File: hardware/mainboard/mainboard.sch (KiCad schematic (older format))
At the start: 29 parts, among them J1 2309407-1, J3 Conn_01x02_Male, J4 3-84953-0, J5 503182-1852, U2 MIC5504-1.2YM5-TR, U5 ICM-20602

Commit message: start on v0.2
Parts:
- J4: footprint mainboard:TE_3-84953-0 -> mainboard:68713014522
- U3: renamed from U?; footprint DFN8_2x3MC_MCH -> mainboard:MCP1725-ADJE_MC
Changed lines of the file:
@@
 NoConn ~ 2750 1100
 NoConn ~ 2750 1200
-Text Notes 7350 4600 0    50   ~ 0
+Text Notes 6200 7900 0    50   ~ 0
 OV13850 FPC Conn\n
 $Comp
@@
 F 0 "J4" H 6980 6046 50  0000 L CNN
 F 1 "3-84953-0" H 6980 5955 50  0000 L CNN
-F 2 "mainboard:TE_3-84953-0" H 6750 6050 50  0001 L BNN
+F 2 "mainboard:68713014522" H 6750 6050 50  0001 L BNN
 F 3 "3-84953-0" H 6750 6050 50  0001 L BNN
 F 4 "Compliant" H 6750 6050 50  0001 L BNN "Field4"
@@
 NoConn ~ 10500 7150
 $Comp
-L power:GND #PWR?
+L power:GND #PWR0235
 U 1 1 5FA58E8D
 P 8500 7450
-F 0 "#PWR?" H 8500 7200 50  0001 C CNN
+F 0 "#PWR0235" H 8500 7200 50  0001 C CNN
 F 1 "GND" H 8505 7277 50  0000 C CNN
 F 2 "" H 8500 7450 50  0001 C CNN
@@
 	8500 7150 8500 7250
 $Comp
-L mainboard:MCP1725-ADJE_MC U?
+L mainboard:MCP1725-ADJE_MC U3
 U 1 1 5F9F70E9
 P 8500 7150
-F 0 "U?" H 9500 7537 60  0000 C CNN
+F 0 "U3" H 9500 7537 60  0000 C CNN
 F 1 "MCP1725-ADJE_MC" H 9500 7431 60  0000 C CNN
-F 2 "DFN8_2x3MC_MCH" H 9500 7390 60  0001 C CNN
+F 2 "mainboard:MCP1725-ADJE_MC" H 9500 7390 60  0001 C CNN
 F 3 "" H 8500 7150 60  0000 C CNN
 	1    8500 7150
@@
 $EndComp
 $Comp
-L power:+3.3V #PWR?
+L power:+3.3V #PWR0236
 U 1 1 5FB39ABE
 P 8150 7150
-F 0 "#PWR?" H 8150 7000 50  0001 C CNN
+F 0 "#PWR0236" H 8150 7000 50  0001 C CNN
 F 1 "+3.3V" V 8165 7278 50  0000 L CNN
 F 2 "" H 8150 7150 50  0001 C CNN
@@
 	11100 7100 11400 7100
 $Comp
-L power:GND #PWR?
+L power:GND #PWR0240
 U 1 1 5FBE8000
 P 11100 6900
-F 0 "#PWR?" H 11100 6650 50  0001 C CNN
+F 0 "#PWR0240" H 11100 6650 50  0001 C CNN
 F 1 "GND" H 11105 6727 50  0000 C CNN
 F 2 "" H 11100 6900 50  0001 C CNN

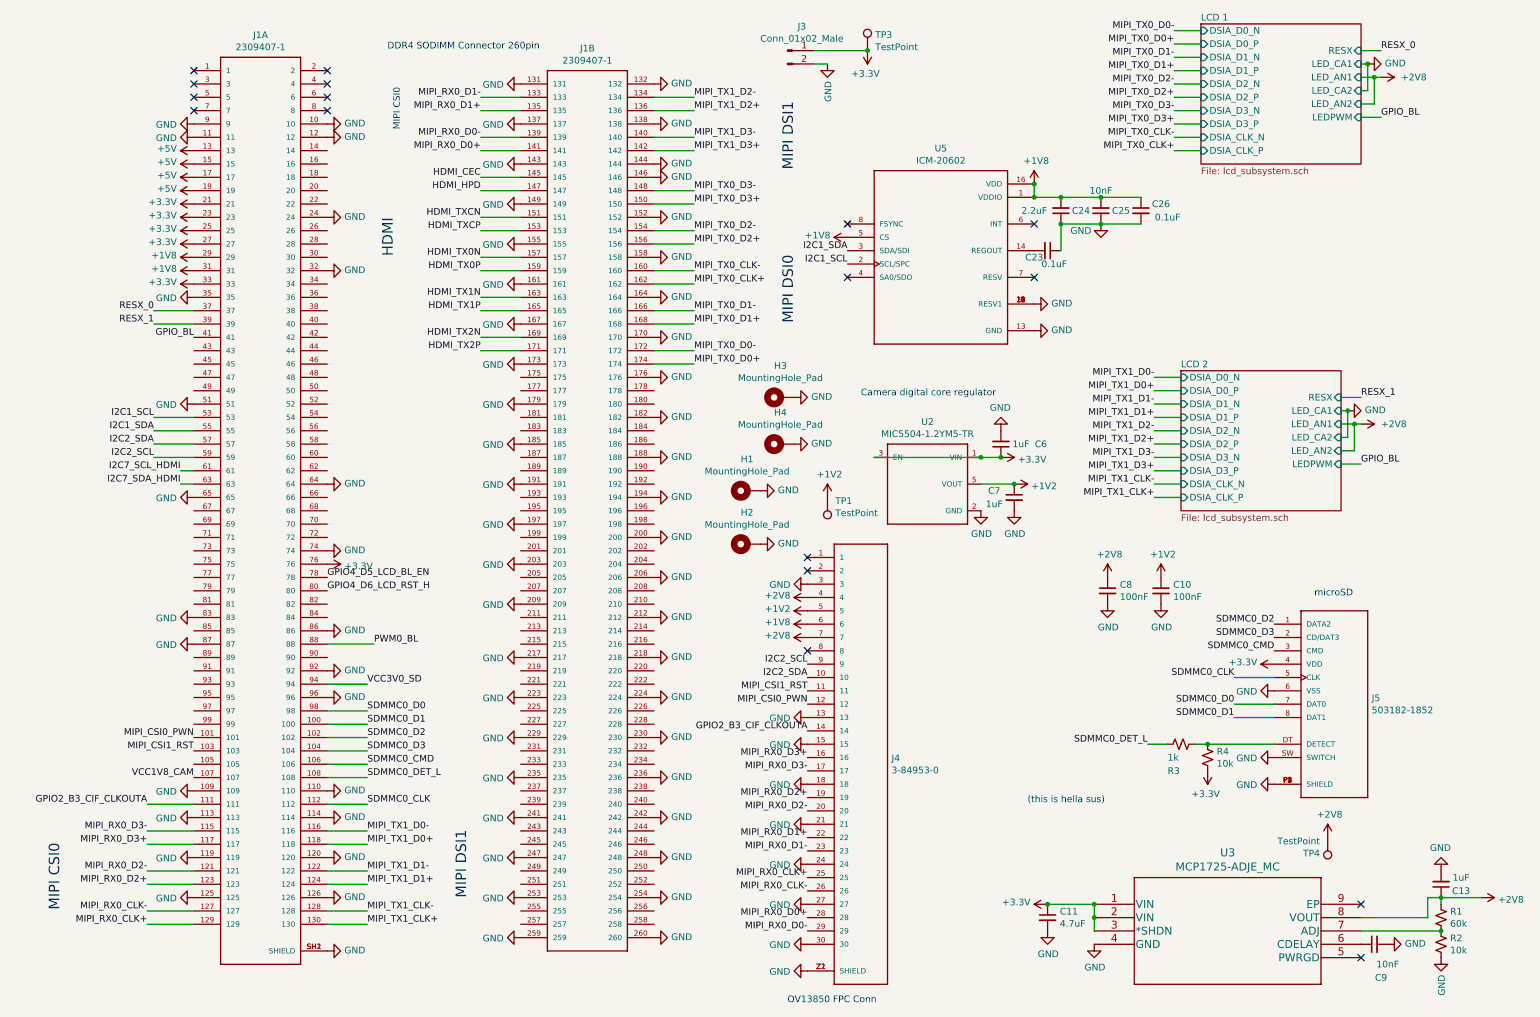
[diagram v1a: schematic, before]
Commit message: redesign started, symbol scripts, new dsi chip
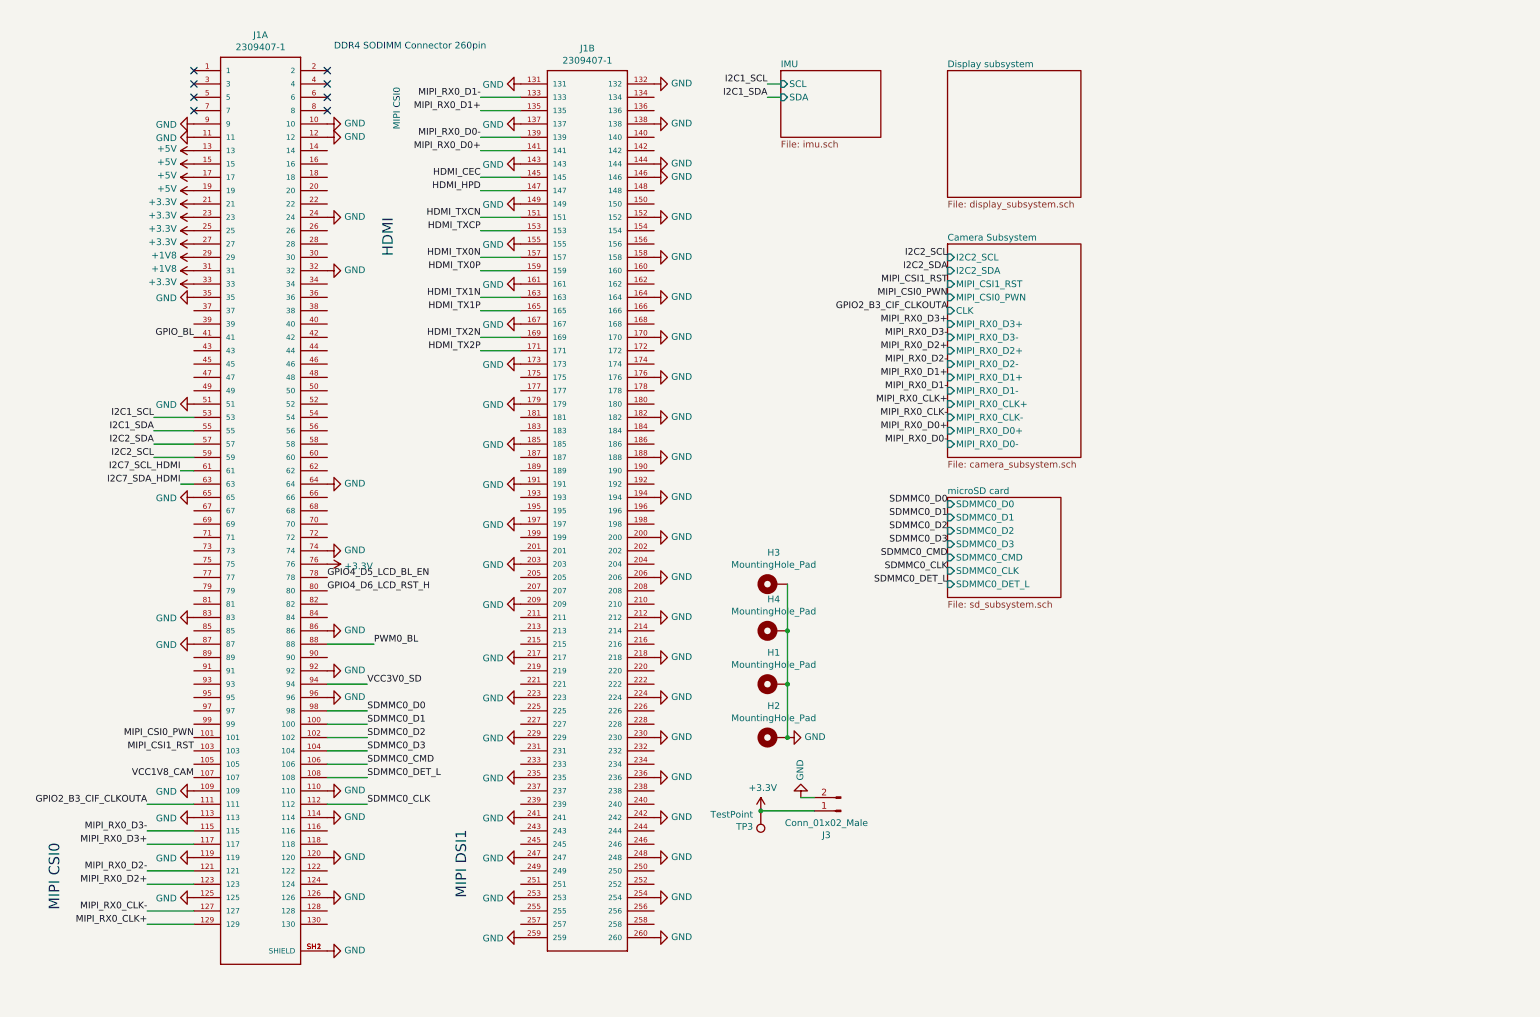
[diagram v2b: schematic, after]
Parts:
- removed C10, C8: 100nF, Capacitor_SMD:C_0402_1005Metric_Pad0.74x0.62mm_HandSolder, symbol Device:C_Small
- removed C11: 4.7uF, Capacitor_SMD:C_0402_1005Metric_Pad0.74x0.62mm_HandSolder, symbol Device:C_Small
- removed C13, C6, C7: 1uF, Capacitor_SMD:C_0402_1005Metric_Pad0.74x0.62mm_HandSolder, symbol Device:C_Small
- removed C23, C26: 0.1uF, Capacitor_SMD:C_0402_1005Metric_Pad0.74x0.62mm_HandSolder, symbol Device:C_Small
- removed C24: 2.2uF, Capacitor_SMD:C_0402_1005Metric_Pad0.74x0.62mm_HandSolder, symbol Device:C_Small
- removed C25, C9: 10nF, Capacitor_SMD:C_0402_1005Metric_Pad0.74x0.62mm_HandSolder, symbol Device:C_Small
- removed J4: 3-84953-0, mainboard:68713014522, symbol mainboard:3-84953-0
- removed J5: 503182-1852, mainboard:MOLEX_503182-1852, symbol mainboard:503182-1852
- removed R1: 60k, Resistor_SMD:R_0402_1005Metric_Pad0.72x0.64mm_HandSolder, symbol Device:R_Small_US
- removed R2, R4: 10k, Resistor_SMD:R_0402_1005Metric_Pad0.72x0.64mm_HandSolder, symbol Device:R_Small_US
- removed R3: 1k, Resistor_SMD:R_0402_1005Metric_Pad0.72x0.64mm_HandSolder, symbol Device:R_Small_US
- removed TP1, TP4: TestPoint, TestPoint:TestPoint_Pad_D1.0mm, symbol Connector:TestPoint
- removed U2: MIC5504-1.2YM5-TR, mainboard:SOT23-5P95_280X145XL45X37N, symbol mainboard:MIC5504-1.2YM5-TR
- removed U3: MCP1725-ADJE_MC, mainboard:MCP1725-ADJE_MC, symbol mainboard:MCP1725-ADJE_MC
- removed U5: ICM-20602, mainboard:PQFN50P300X300X80-16N, symbol mainboard:ICM-20602
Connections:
- net MIPI_TX0_CLK+: no longer names the net of J1.162
- net MIPI_TX0_CLK-: no longer names the net of J1.160
- net MIPI_TX0_D0+: no longer names the net of J1.174
- net MIPI_TX0_D0-: no longer names the net of J1.172
- net MIPI_TX0_D1+: no longer names the net of J1.168
- net MIPI_TX0_D1-: no longer names the net of J1.166
- net MIPI_TX0_D2+: no longer names the net of J1.156
- net MIPI_TX0_D2-: no longer names the net of J1.154
- net MIPI_TX0_D3+: no longer names the net of J1.150
- net MIPI_TX0_D3-: no longer names the net of J1.148
- net MIPI_TX1_CLK+: no longer names the net of J1.130
- net MIPI_TX1_CLK-: no longer names the net of J1.128
- net MIPI_TX1_D0+: no longer names the net of J1.118
- net MIPI_TX1_D0-: no longer names the net of J1.116
- net MIPI_TX1_D1+: no longer names the net of J1.124
- net MIPI_TX1_D1-: no longer names the net of J1.122
- net MIPI_TX1_D2+: no longer names the net of J1.136
- net MIPI_TX1_D2-: no longer names the net of J1.134
- net MIPI_TX1_D3+: no longer names the net of J1.142
- net MIPI_TX1_D3-: no longer names the net of J1.140
- net RESX_0: no longer names the net of J1.37
- net RESX_1: no longer names the net of J1.39
- no-connect marks 17 -> 8
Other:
- note removed: "(this is hella sus)"
- note removed: "Camera digital core regulator\n"
- note removed: "MIPI DSI0"
- note removed: "MIPI DSI1\n"
- note removed: "OV13850 FPC Conn\n"
- note removed: "microSD\n"
- moved on the sheet: H1, H2, H3, H4, J3, TP3

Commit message: finish sch arch, remove coproc, add bl driver, need to do TC power supply
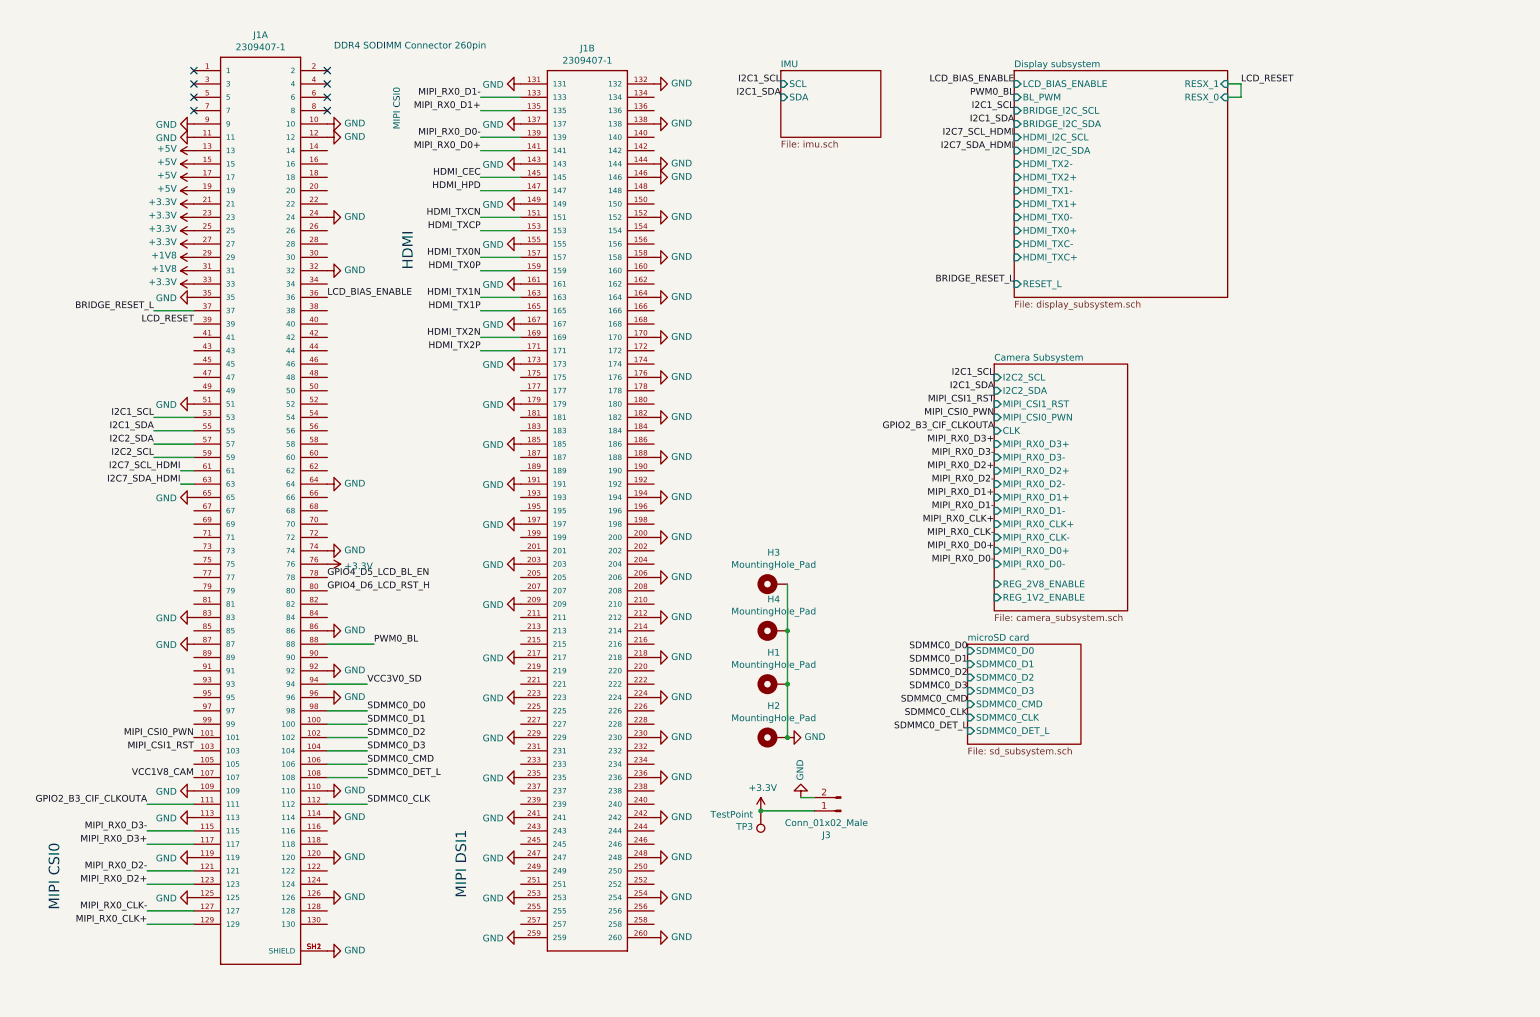
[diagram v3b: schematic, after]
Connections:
- net LCD_BIAS_ENABLE: now reaches J1.36
- net BRIDGE_RESET_L: now reaches J1.37
- net LCD_RESET: now reaches J1.39
- net GPIO_BL: no longer names the net of J1.41
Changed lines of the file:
@@
 Text Notes 3300 1350 1    50   ~ 0
 MIPI CSI0\n
-Text Notes 3250 2300 1    79   ~ 0
+Text Notes 3400 2400 1    79   ~ 0
 HDMI\n
 $Comp
@@
 Text Notes 3800 6600 3    79   ~ 0
 MIPI DSI1
-Text Label 1750 2900 2    50   ~ 0
-GPIO_BL
 Text Label 1450 3500 2    50   ~ 0
 I2C1_SCL
@@
 Wire Wire Line
 	1450 3800 1750 3800
-Text Label 6050 1000 2    50   ~ 0
+Text Label 6150 1000 2    50   ~ 0
 I2C1_SCL
-Text Label 6050 1100 2    50   ~ 0
+Text Label 6150 1100 2    50   ~ 0
 I2C1_SDA
 $Comp
@@
 F3 "SDA" I L 6150 1100 50
 $EndSheet
-Wire Wire Line
-	6050 1000 6150 1000
-Wire Wire Line
-	6050 1100 6150 1100
 $Sheet
-S 7400 900  1000 950
+S 7900 900  1600 1700
 U 5FF71A49
 F0 "Display subsystem" 50
 F1 "display_subsystem.sch" 50
+F2 "LCD_BIAS_ENABLE" I L 7900 1000 50
+F3 "RESET_L" I L 7900 2500 50
+F4 "HDMI_TXC+" I L 7900 2300 50
+F5 "HDMI_TXC-" I L 7900 2200 50
+F6 "HDMI_TX0+" I L 7900 2100 50
+F7 "HDMI_TX0-" I L 7900 2000 50
+F8 "HDMI_TX1+" I L 7900 1900 50
+F9 "HDMI_TX1-" I L 7900 1800 50
+F10 "HDMI_TX2+" I L 7900 1700 50
+F11 "HDMI_TX2-" I L 7900 1600 50
+F12 "HDMI_I2C_SDA" I L 7900 1500 50
+F13 "HDMI_I2C_SCL" I L 7900 1400 50
+F14 "BRIDGE_I2C_SDA" I L 7900 1300 50
+F15 "BRIDGE_I2C_SCL" I L 7900 1200 50
+F16 "BL_PWM" I L 7900 1100 50
+F17 "RESX_1" I R 9500 1000 50
+F18 "RESX_0" I R 9500 1100 50
 $EndSheet
-Text Label 7400 2600 2    50   ~ 0
+Text Label 7750 3500 2    50   ~ 0
 MIPI_CSI0_PWN
-Text Label 7400 2800 2    50   ~ 0
+Text Label 7750 3700 2    50   ~ 0
 MIPI_RX0_D3+
-Text Label 7400 2900 2    50   ~ 0
+Text Label 7750 3800 2    50   ~ 0
 MIPI_RX0_D3-
-Text Label 7400 3000 2    50   ~ 0
+Text Label 7750 3900 2    50   ~ 0
 MIPI_RX0_D2+
-Text Label 7400 3100 2    50   ~ 0
+Text Label 7750 4000 2    50   ~ 0
 MIPI_RX0_D2-
-Text Label 7400 3200 2    50   ~ 0
+Text Label 7750 4100 2    50   ~ 0
 MIPI_RX0_D1+
-Text Label 7400 3300 2    50   ~ 0
+Text Label 7750 4200 2    50   ~ 0
 MIPI_RX0_D1-
-Text Label 7400 3600 2    50   ~ 0
+Text Label 7750 4500 2    50   ~ 0
 MIPI_RX0_D0+
-Text Label 7400 3700 2    50   ~ 0
+Text Label 7750 4600 2    50   ~ 0
 MIPI_RX0_D0-
-Text Label 7400 3400 2    50   ~ 0
+Text Label 7750 4300 2    50   ~ 0
 MIPI_RX0_CLK+
-Text Label 7400 3500 2    50   ~ 0
+Text Label 7750 4400 2    50   ~ 0
 MIPI_RX0_CLK-
-Text Label 7400 2700 2    50   ~ 0
+Text Label 7750 3600 2    50   ~ 0
 GPIO2_B3_CIF_CLKOUTA
-Text Label 7400 2400 2    50   ~ 0
-I2C2_SDA
-Text Label 7400 2300 2    50   ~ 0
-I2C2_SCL
-Text Label 7400 2500 2    50   ~ 0
+Text Label 7750 3400 2    50   ~ 0
 MIPI_CSI1_RST
 $Sheet
-S 7400 2200 1000 1600
+S 7750 3100 1000 1850
 U 5FFAA2CE
 F0 "Camera Subsystem" 50
 F1 "camera_subsystem.sch" 50
-F2 "MIPI_RX0_D0-" I L 7400 3700 50
-F3 "MIPI_RX0_D0+" I L 7400 3600 50
-F4 "MIPI_RX0_CLK-" I L 7400 3500 50
-F5 "MIPI_RX0_CLK+" I L 7400 3400 50
-F6 "MIPI_RX0_D1-" I L 7400 3300 50
-F7 "MIPI_RX0_D1+" I L 7400 3200 50
-F8 "MIPI_RX0_D2-" I L 7400 3100 50
-F9 "MIPI_RX0_D2+" I L 7400 3000 50
-F10 "MIPI_RX0_D3-" I L 7400 2900 50
-F11 "MIPI_RX0_D3+" I L 7400 2800 50
-F12 "CLK" I L 7400 2700 50
-F13 "MIPI_CSI0_PWN" I L 7400 2600 50
-F14 "MIPI_CSI1_RST" I L 7400 2500 50
-F15 "I2C2_SDA" I L 7400 2400 50
-F16 "I2C2_SCL" I L 7400 2300 50
+F2 "MIPI_RX0_D0-" I L 7750 4600 50
+F3 "MIPI_RX0_D0+" I L 7750 4500 50
+F4 "MIPI_RX0_CLK-" I L 7750 4400 50
+F5 "MIPI_RX0_CLK+" I L 7750 4300 50
+F6 "MIPI_RX0_D1-" I L 7750 4200 50
+F7 "MIPI_RX0_D1+" I L 7750 4100 50
+F8 "MIPI_RX0_D2-" I L 7750 4000 50
+F9 "MIPI_RX0_D2+" I L 7750 3900 50
+F10 "MIPI_RX0_D3-" I L 7750 3800 50
+F11 "MIPI_RX0_D3+" I L 7750 3700 50
+F12 "CLK" I L 7750 3600 50
+F13 "MIPI_CSI0_PWN" I L 7750 3500 50
+F14 "MIPI_CSI1_RST" I L 7750 3400 50
+F15 "I2C2_SDA" I L 7750 3300 50
+F16 "I2C2_SCL" I L 7750 3200 50
+F17 "REG_2V8_ENABLE" I L 7750 4750 50
+F18 "REG_1V2_ENABLE" I L 7750 4850 50
 $EndSheet
 $Sheet
-S 7400 4100 850  750
+S 7550 5200 850  750
 U 601227A6
 F0 "microSD card" 50
 F1 "sd_subsystem.sch" 50
-F2 "SDMMC0_D2" I L 7400 4350 50
-F3 "SDMMC0_D3" I L 7400 4450 50
-F4 "SDMMC0_CMD" I L 7400 4550 50
-F5 "SDMMC0_CLK" I L 7400 4650 50
-F6 "SDMMC0_D0" I L 7400 4150 50
-F7 "SDMMC0_D1" I L 7400 4250 50
-F8 "SDMMC0_DET_L" I L 7400 4750 50
+F2 "SDMMC0_D2" I L 7550 5450 50
+F3 "SDMMC0_D3" I L 7550 5550 50
+F4 "SDMMC0_CMD" I L 7550 5650 50
+F5 "SDMMC0_CLK" I L 7550 5750 50
+F6 "SDMMC0_D0" I L 7550 5250 50
+F7 "SDMMC0_D1" I L 7550 5350 50
+F8 "SDMMC0_DET_L" I L 7550 5850 50
 $EndSheet
-Text Label 7400 4150 2    50   ~ 0
+Text Label 7550 5250 2    50   ~ 0
 SDMMC0_D0
-Text Label 7400 4250 2    50   ~ 0
+Text Label 7550 5350 2    50   ~ 0
 SDMMC0_D1
-Text Label 7400 4450 2    50   ~ 0
+Text Label 7550 5550 2    50   ~ 0
 SDMMC0_D3
-Text Label 7400 4550 2    50   ~ 0
+Text Label 7550 5650 2    50   ~ 0
 SDMMC0_CMD
-Text Label 7400 4750 2    50   ~ 0
+Text Label 7550 5850 2    50   ~ 0
 SDMMC0_DET_L
-Text Label 7400 4650 2    50   ~ 0
+Text Label 7550 5750 2    50   ~ 0
 SDMMC0_CLK
-Text Label 7400 4350 2    50   ~ 0
+Text Label 7550 5450 2    50   ~ 0
 SDMMC0_D2
+Text Label 7750 3200 2    50   ~ 0
+I2C1_SCL
+Text Label 7750 3300 2    50   ~ 0
+I2C1_SDA
+Text Label 7900 1000 2    50   ~ 0
+LCD_BIAS_ENABLE
+Text Label 2750 2600 0    50   ~ 0
+LCD_BIAS_ENABLE
+Text Label 7900 1100 2    50   ~ 0
+PWM0_BL
+Text Label 7900 1200 2    50   ~ 0
+I2C1_SCL
+Text Label 7900 1300 2    50   ~ 0
+I2C1_SDA
+Text Label 7900 1400 2    50   ~ 0
+I2C7_SCL_HDMI
+Text Label 7900 1500 2    50   ~ 0
+I2C7_SDA_HDMI
+Text Label 7900 2500 2    50   ~ 0
+BRIDGE_RESET_L
+Text Label 1450 2700 2    50   ~ 0
+BRIDGE_RESET_L
+Wire Wire Line
+	1450 2700 1750 2700
+Text Label 1750 2800 2    50   ~ 0
+LCD_RESET
+Text Label 9600 1000 0    50   ~ 0
+LCD_RESET
+Wire Wire Line
+	9500 1000 9600 1000
+Wire Wire Line
+	9500 1100 9600 1100
+Wire Wire Line
+	9600 1100 9600 1000
 $EndSCHEMATC
